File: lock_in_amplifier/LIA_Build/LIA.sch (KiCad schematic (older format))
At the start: 35 parts, among them J10 A IN, J11 B IN, J12 POWER_IN, J13 A IN, J14 I IN, J15 I IN, J16 TEST EN, J17 1E9 TEST, J18 1E6 TEST, J19 1E3 TEST, J20 AMP OUT, J21 AMP OUT, J22 CLK IN, J23 CLK IN, J24 PHASE OUT, J25 MAGNITUDE OUT, J26 CLK OUT, J27 CLK OUT, J28 PHASE OUT, J29 MAGNITUDE OUT, J30 DEMOD OUT - I, J31 DEMOD OUT I, J32 DEMOD OUT Q, J33 DEMOD OUT - Q, J34 LFP OUT - Q, J35 LPF OUT - I, J36 LFP OUT Q, J37 LFP OUT I, J9 B IN

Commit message: power supply, amp chain first pass
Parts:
- removed J16: TEST EN, symbol TEST_2P
- removed J17: 1E9 TEST, symbol TEST_2P
- removed J18: 1E6 TEST, symbol TEST_2P
- removed J19: 1E3 TEST, symbol TEST_2P
- removed J24: PHASE OUT, symbol Conn_01x01
- removed J25: MAGNITUDE OUT, symbol Conn_01x01
- removed J28: PHASE OUT, symbol Conn_Coaxial
- removed J29: MAGNITUDE OUT, symbol Conn_Coaxial
- removed J34: LFP OUT - Q, symbol TEST_2P
- removed J35: LPF OUT - I, symbol TEST_2P
- removed J36: LFP OUT Q, symbol Conn_Coaxial
- removed J37: LFP OUT I, symbol Conn_Coaxial
- added J16: TEST SIGNAL OUT, Pin_Headers:Pin_Header_Straight_1x01_Pitch1.00mm, symbol TEST_1P
- added J17: TEST LOW SIDE VALUE, Pin_Headers:Pin_Header_Straight_1x03_Pitch2.54mm, symbol Conn_01x03
- added J18: TEST HIGH SIDE VALUE, Pin_Headers:Pin_Header_Straight_2x05_Pitch2.54mm, symbol Conn_02x05_Counter_Clockwise
- added R35: 1G, symbol R
- added R36: 1M, Resistors_SMD:R_0805, symbol R
- J10: value A IN -> A IN COAX; footprint (none) -> Connectors:SMA_THT_Jack_Straight
- J11, J13, J15, J20, J22, J26, J30, J33: footprint (none) -> Pin_Headers:Pin_Header_Straight_1x02_Pitch2.54mm
- J14: value I IN -> I IN COAX; footprint (none) -> Connectors:SMA_THT_Jack_Straight
- J21: value AMP OUT -> AMP OUT COAX; footprint (none) -> Connectors:SMA_THT_Jack_Straight
- J23: value CLK IN -> CLK IN COAX; footprint (none) -> Connectors:SMA_THT_Jack_Straight
- J27: value CLK OUT -> CLK OUT COAX; footprint (none) -> Connectors:SMA_THT_Jack_Straight
- J31: value DEMOD OUT I -> DEMOD OUT I COAX; footprint (none) -> Connectors:SMA_THT_Jack_Straight
- J32: value DEMOD OUT Q -> DEMOD OUT Q COAX; footprint (none) -> Connectors:SMA_THT_Jack_Straight
- J9: value B IN -> B IN COAX; footprint (none) -> Connectors:SMA_THT_Jack_Straight
- R10: value 0.1 -> 1; footprint (none) -> Resistors_SMD:R_0805
- R11: value 1 -> .1; footprint (none) -> Resistors_SMD:R_0805
- R12, R13, R14, R15: footprint (none) -> Resistors_SMD:R_0805
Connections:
- wire segments 71 -> 80
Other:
- note added: "DFM TODO:\nRESISTOR COMP. CT. MINIMIZATION\nMANUFACTURE TP. PLACEMENT.\nMANUFACTURE 0 OHM"
- note added: "GUARD TRACES AROUND HIGH IMPEDANCE PATHS"
- note added: "MAJOR TODO:\nSELECT TRANSIMPEDANCE AMP\nAMPLIFIER NOISE TRADES - WRITEUP / VERIFY\nPLL SELECTION\nLINE FILTER DESIGN"
- note added: "◦ Work noise budget!\n"
- note removed: "maybe? may involve MCU\nin wich case maybe not?"
- note removed: "• Output integration / lpf\n ◦ Switched time constant / output buffer\n ▪ Long time constants (~10s) desireable\n ▪ 10hz,1hz,1s,10s - 100s possible?\n"
- note removed: "◦ Work noise budget!\n ◦ Test point selection\n ▪ 100 mil header\n ▪ 0603 probe pads - https://www.digikey.com/product-detail/en/te-connectivity-amp-connectors/RCT-0C/A106144CT-ND/3477801 \n ▪ Get rid of ground pigtails somehow?\n ▪ Mmcx connectors - $$$\n ◦ Connector selection\n ▪ BNC - edge mount\n ▪ SMA - edge mount\n ▪ 100 mil headers\nIndicators, dials, connectors, etc. start looking at bein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"
- moved on the sheet: J26, J27, J30, J31, J32, J33, R10, R12, R13, R14, R15

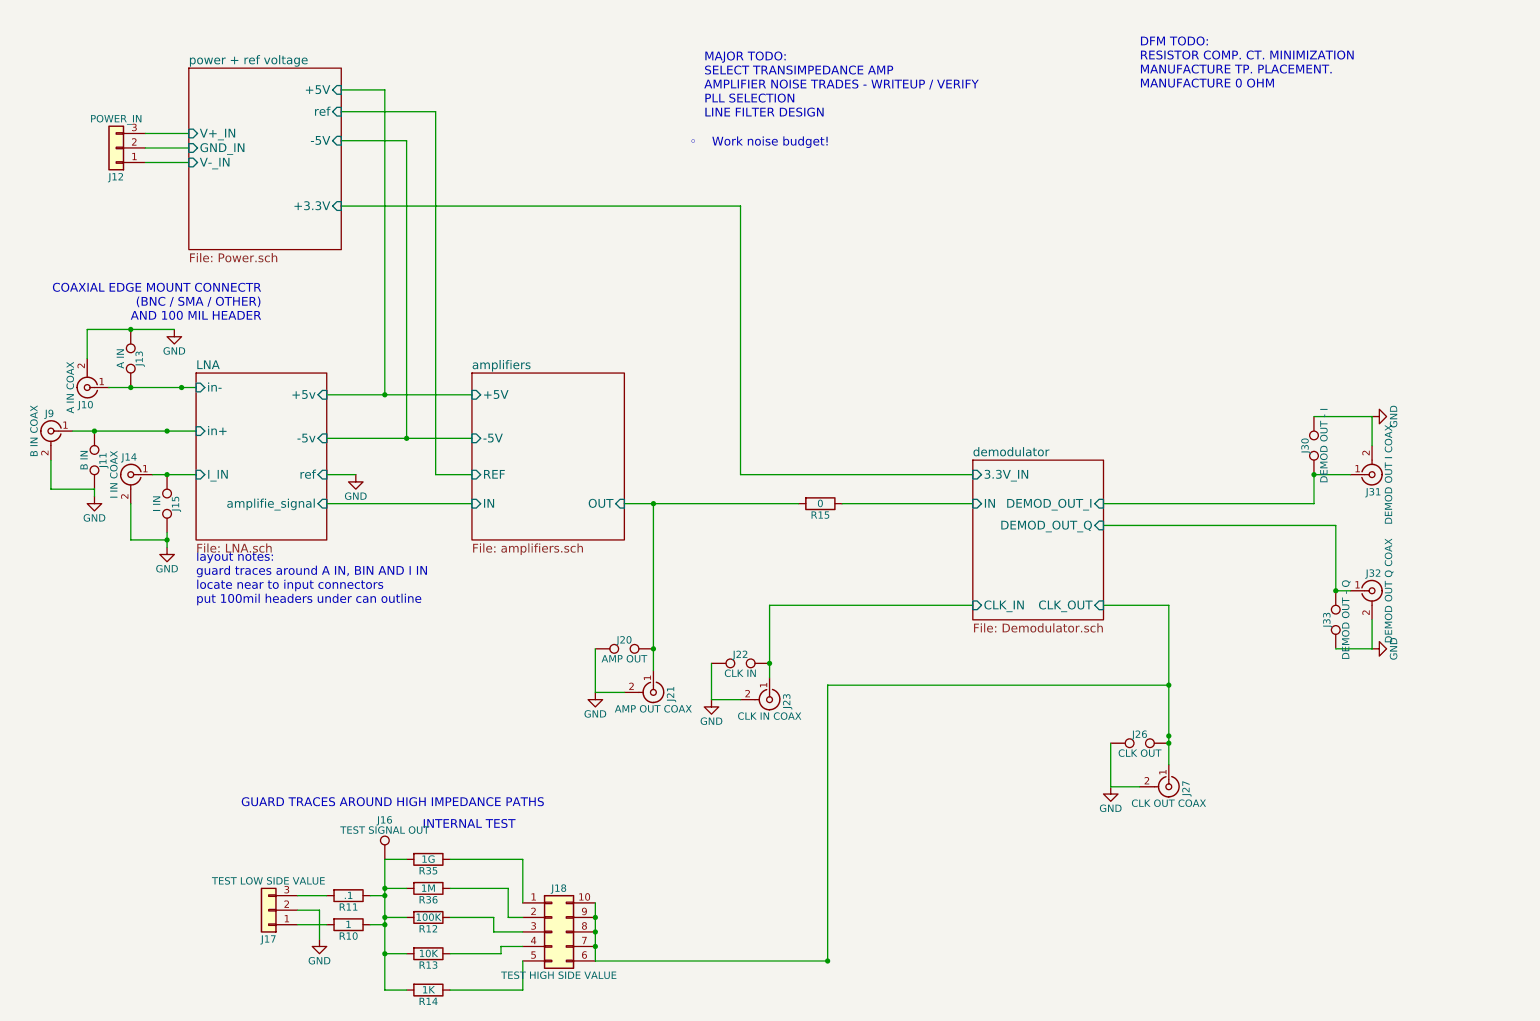
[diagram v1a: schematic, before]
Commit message: initial transimpedance selection, lna refinement
amp overload led
switch comps added
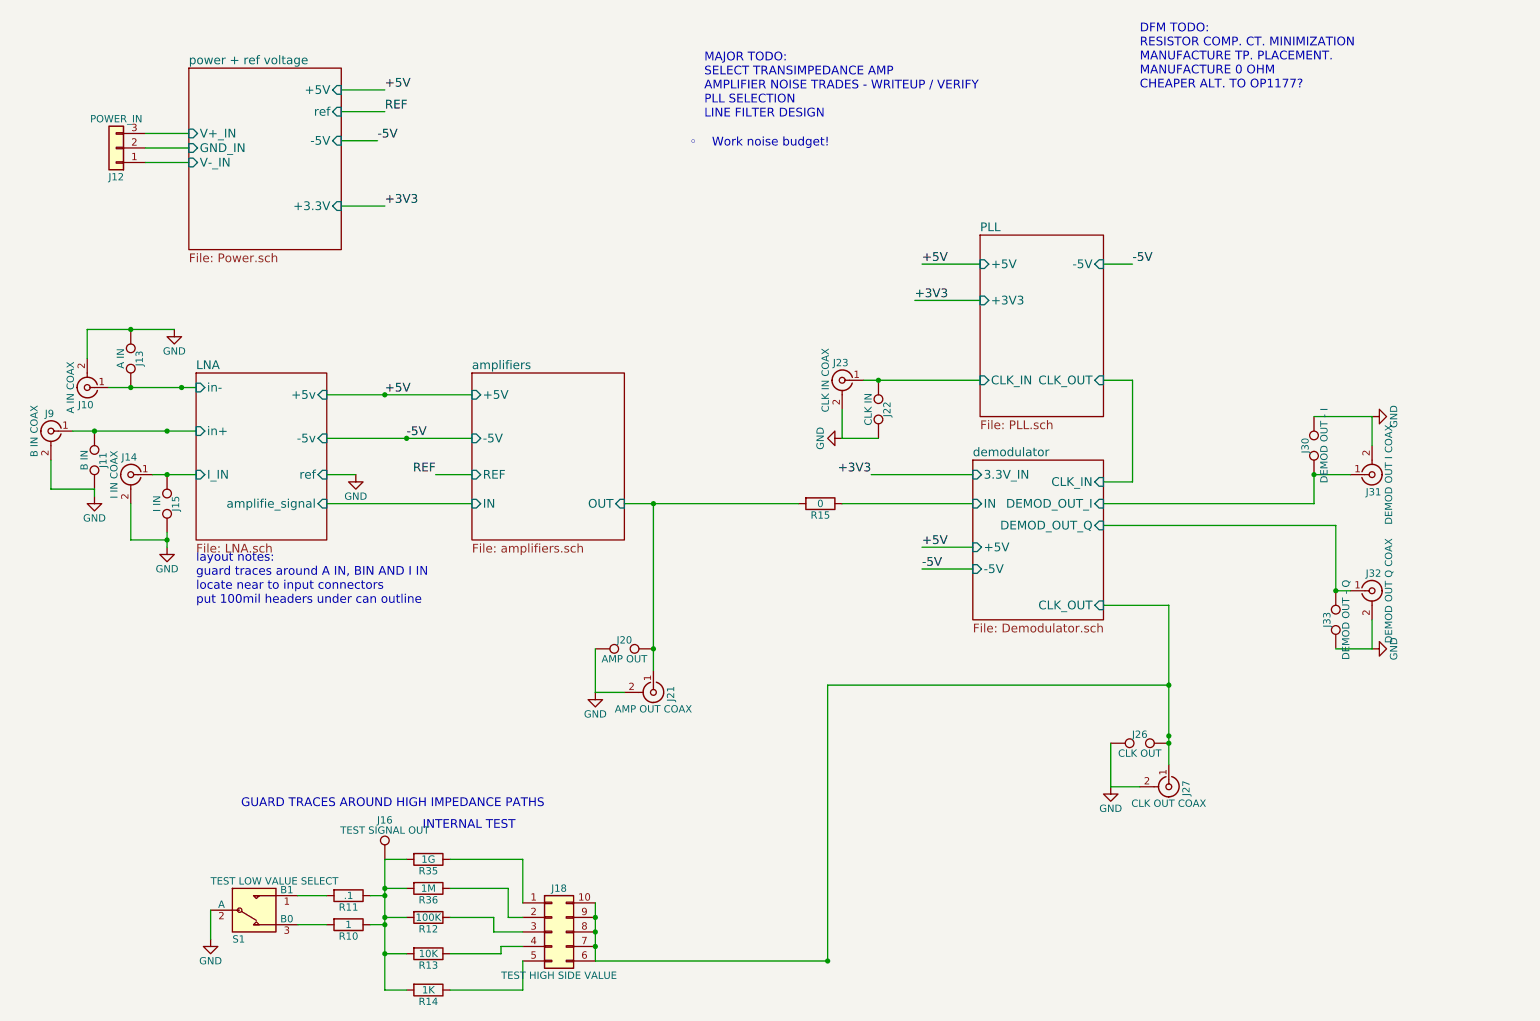
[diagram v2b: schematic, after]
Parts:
- removed J17: TEST LOW SIDE VALUE, Pin_Headers:Pin_Header_Straight_1x03_Pitch2.54mm, symbol Conn_01x03
- added S1: TEST LOW VALUE SELECT, symbol SPDT
- R35: footprint (none) -> Resistors_THT:R_Axial_DIN0414_L11.9mm_D4.5mm_P15.24mm_Horizontal
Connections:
- net GND: now also S1.2 (A)
- net at R10.2: now also S1.3 (B0)
- net at R11.2: now also S1.1 (B1)
- net demodulator/CLK_IN renamed PLL/CLK_IN
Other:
- note added: "DFM TODO:\nRESISTOR COMP. CT. MINIMIZATION\nMANUFACTURE TP. PLACEMENT.\nMANUFACTURE 0 OHM \nCHEAPER ALT. TO OP1177?"
- note removed: "COAXIAL EDGE MOUNT CONNECTR \n(BNC / SMA / OTHER)\nAND 100 MIL HEADER"
- note removed: "DFM TODO:\nRESISTOR COMP. CT. MINIMIZATION\nMANUFACTURE TP. PLACEMENT.\nMANUFACTURE 0 OHM"
- moved on the sheet: J22, J23

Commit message: switch footprints, lm833 usage, pll investigation
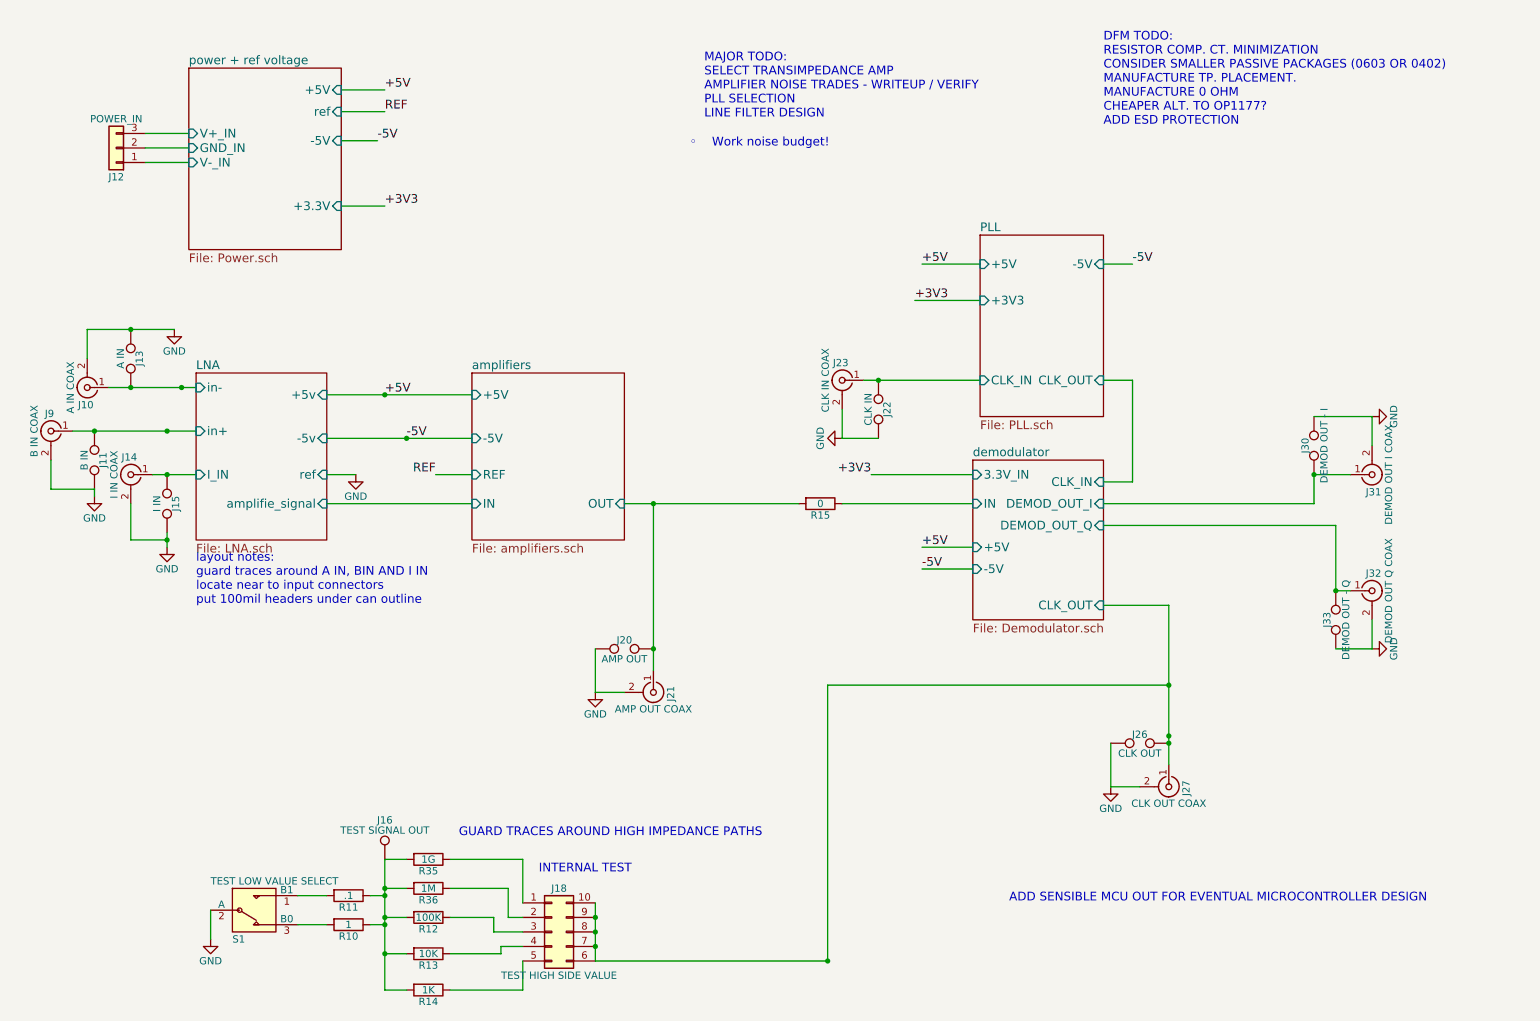
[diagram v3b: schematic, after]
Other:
- note added: "ADD SENSIBLE MCU OUT FOR EVENTUAL MICROCONTROLLER DESIGN"
- note added: "DFM TODO:\nRESISTOR COMP. CT. MINIMIZATION\nCONSIDER SMALLER PASSIVE PACKAGES (0603 OR 0402)\nMANUFACTURE TP. PLACEMENT.\nMANUFACTURE 0 OHM \nCHEAPER ALT. TO OP1177?\nADD ESD PROTECTION"
- note removed: "DFM TODO:\nRESISTOR COMP. CT. MINIMIZATION\nMANUFACTURE TP. PLACEMENT.\nMANUFACTURE 0 OHM \nCHEAPER ALT. TO OP1177?"
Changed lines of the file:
@@
 	1    0    0    -1
 $EndComp
-Text Notes 3850 6100 2    60   ~ 0
+Text Notes 4650 6400 2    60   ~ 0
 INTERNAL TEST
 $Comp
@@
 	1    0    0    -1
 $EndComp
-Text Notes 4050 5950 2    60   ~ 0
+Text Notes 5550 6150 2    60   ~ 0
 GUARD TRACES AROUND HIGH IMPEDANCE PATHS
 Text Notes 5150 1200 0    60   ~ 0
 MAJOR TODO:\nSELECT TRANSIMPEDANCE AMP\nAMPLIFIER NOISE TRADES - WRITEUP / VERIFY\nPLL SELECTION\nLINE FILTER DESIGN
-Text Notes 8150 1000 0    60   ~ 0
-DFM TODO:\nRESISTOR COMP. CT. MINIMIZATION\nMANUFACTURE TP. PLACEMENT.\nMANUFACTURE 0 OHM \nCHEAPER ALT. TO OP1177?
+Text Notes 7900 1250 0    60   ~ 0
+DFM TODO:\nRESISTOR COMP. CT. MINIMIZATION\nCONSIDER SMALLER PASSIVE PACKAGES (0603 OR 0402)\nMANUFACTURE TP. PLACEMENT.\nMANUFACTURE 0 OHM \nCHEAPER ALT. TO OP1177?\nADD ESD PROTECTION
 $Comp
 L SPDT S1
@@
 Wire Wire Line
 	6650 4150 7000 4150
+Text Notes 7250 6600 0    60   ~ 0
+ADD SENSIBLE MCU OUT FOR EVENTUAL MICROCONTROLLER DESIGN
 $EndSCHEMATC

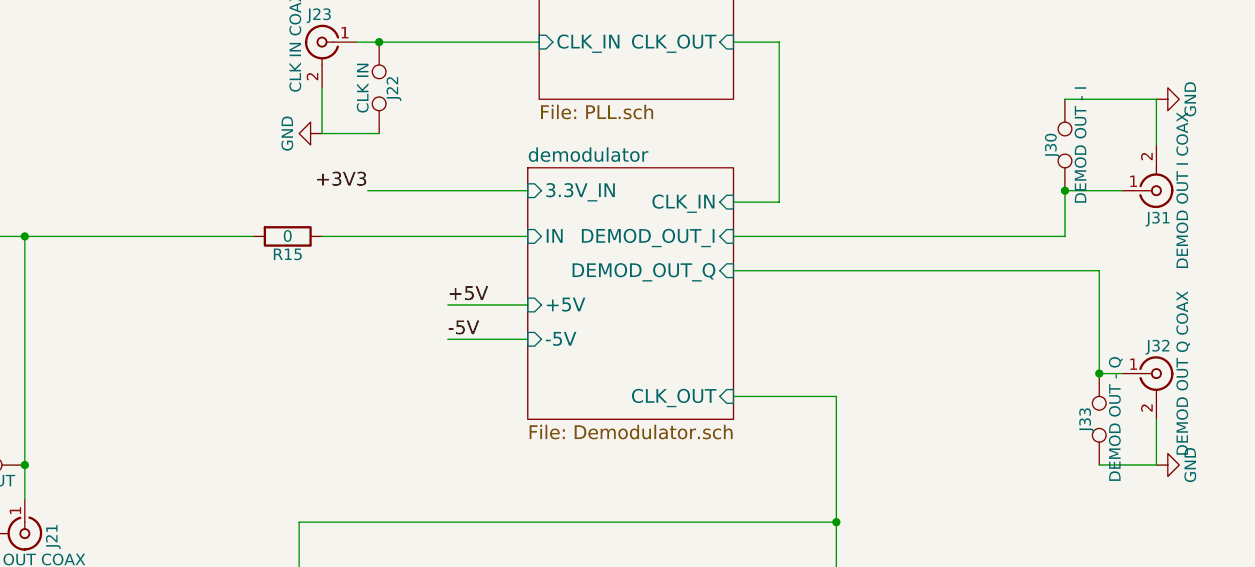
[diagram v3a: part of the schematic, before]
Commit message: PLL initial implementation
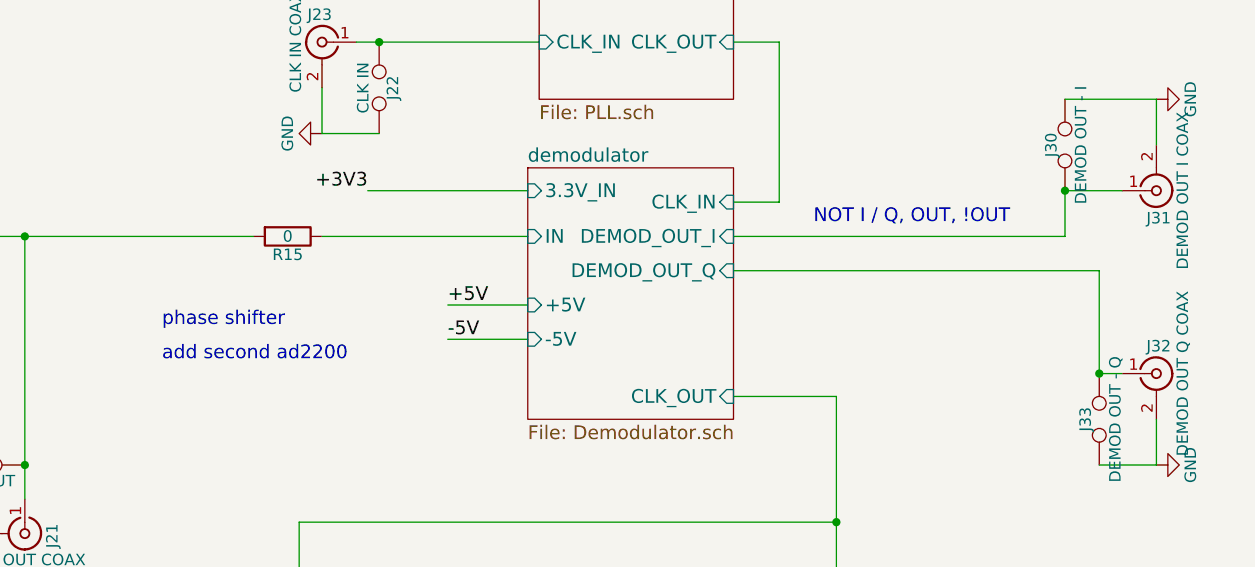
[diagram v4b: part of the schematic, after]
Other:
- note added: "NOT I / Q, OUT, !OUT"
- note added: "add second ad2200"
- note added: "phase shifter"
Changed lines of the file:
@@
 $EndSheet
 $Comp
-L GND #PWR01
+L GND #PWR5
 U 1 1 5A1F9691
 P 2750 3650
-F 0 "#PWR01" H 2750 3400 50  0001 C CNN
+F 0 "#PWR5" H 2750 3400 50  0001 C CNN
 F 1 "GND" H 2750 3500 50  0000 C CNN
 F 2 "" H 2750 3650 50  0001 C CNN
@@
 $EndComp
 $Comp
-L GND #PWR02
+L GND #PWR3
 U 1 1 5A2003C9
 P 1500 2650
-F 0 "#PWR02" H 1500 2400 50  0001 C CNN
+F 0 "#PWR3" H 1500 2400 50  0001 C CNN
 F 1 "GND" H 1500 2500 50  0000 C CNN
 F 2 "" H 1500 2650 50  0001 C CNN
@@
 $EndComp
 $Comp
-L GND #PWR03
+L GND #PWR2
 U 1 1 5A2004F1
 P 1450 4150
-F 0 "#PWR03" H 1450 3900 50  0001 C CNN
+F 0 "#PWR2" H 1450 3900 50  0001 C CNN
 F 1 "GND" H 1450 4000 50  0000 C CNN
 F 2 "" H 1450 4150 50  0001 C CNN
@@
 $EndComp
 $Comp
-L GND #PWR04
+L GND #PWR1
 U 1 1 5A20072D
 P 950 3800
-F 0 "#PWR04" H 950 3550 50  0001 C CNN
+F 0 "#PWR1" H 950 3550 50  0001 C CNN
 F 1 "GND" H 950 3650 50  0000 C CNN
 F 2 "" H 950 3800 50  0001 C CNN
@@
 $EndComp
 $Comp
-L GND #PWR05
+L GND #PWR6
 U 1 1 5A203CBF
 P 4400 5150
-F 0 "#PWR05" H 4400 4900 50  0001 C CNN
+F 0 "#PWR6" H 4400 4900 50  0001 C CNN
 F 1 "GND" H 4400 5000 50  0000 C CNN
 F 2 "" H 4400 5150 50  0001 C CNN
@@
 $EndComp
 $Comp
-L GND #PWR06
+L GND #PWR7
 U 1 1 5A203EC2
 P 6100 3400
-F 0 "#PWR06" H 6100 3150 50  0001 C CNN
+F 0 "#PWR7" H 6100 3150 50  0001 C CNN
 F 1 "GND" H 6100 3250 50  0000 C CNN
 F 2 "" H 6100 3400 50  0001 C CNN
@@
 $EndComp
 $Comp
-L GND #PWR07
+L GND #PWR8
 U 1 1 5A203FFF
 P 7950 5800
-F 0 "#PWR07" H 7950 5550 50  0001 C CNN
+F 0 "#PWR8" H 7950 5550 50  0001 C CNN
 F 1 "GND" H 7950 5650 50  0000 C CNN
 F 2 "" H 7950 5800 50  0001 C CNN
@@
 $EndComp
 $Comp
-L GND #PWR08
+L GND #PWR9
 U 1 1 5A20451A
 P 9750 3250
-F 0 "#PWR08" H 9750 3000 50  0001 C CNN
+F 0 "#PWR9" H 9750 3000 50  0001 C CNN
 F 1 "GND" H 9750 3100 50  0000 C CNN
 F 2 "" H 9750 3250 50  0001 C CNN
@@
 $EndComp
 $Comp
-L GND #PWR09
+L GND #PWR10
 U 1 1 5A204657
 P 9750 4850
-F 0 "#PWR09" H 9750 4600 50  0001 C CNN
+F 0 "#PWR10" H 9750 4600 50  0001 C CNN
 F 1 "GND" H 9750 4700 50  0000 C CNN
 F 2 "" H 9750 4850 50  0001 C CNN
@@
 $EndComp
 $Comp
-L GND #PWR010
+L GND #PWR4
 U 1 1 5A212B2B
 P 1750 6850
-F 0 "#PWR010" H 1750 6600 50  0001 C CNN
+F 0 "#PWR4" H 1750 6600 50  0001 C CNN
 F 1 "GND" H 1750 6700 50  0000 C CNN
 F 2 "" H 1750 6850 50  0001 C CNN
@@
 Text Notes 7250 6600 0    60   ~ 0
 ADD SENSIBLE MCU OUT FOR EVENTUAL MICROCONTROLLER DESIGN
+Text Notes 5400 4250 0    60   ~ 0
+phase shifter
+Text Notes 8250 3800 0    60   ~ 0
+NOT I / Q, OUT, !OUT
+Text Notes 5400 4400 0    60   ~ 0
+add second ad2200
 $EndSCHEMATC
